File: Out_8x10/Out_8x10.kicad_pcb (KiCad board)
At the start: 2 copper layers, 100 x 100 mm, 162 parts, among them J1 Conn_01x06, J2 nmount SW Debug, J3 USB_C_Receptacle_USB2.0, J4 Conn_01x06, J5 Conn_01x09, J6 Conn_01x10, J7 Conn_01x09, J8 Conn_01x12, Q1 2N7002, Q10 AO3401A, Q11 AO3401A, Q12 AO3401A, Q13 2N7002, Q14 2N7002, Q15 AO3401A, Q16 AO3401A, Q17 AO3400A, Q18 AO3400A, Q19 AO3400A, Q2 2N7002, Q20 AO3400A, Q21 AO3400A, Q22 AO3400A, Q23 AO3400A, Q24 AO3400A, Q25 AO3400A, Q26 AO3400A, Q3 2N7002, Q4 AO3401A, Q5 AO3401A, Q6 AO3401A, Q7 2N7002, Q8 2N7002, Q9 2N7002, SW1 Reset, SW2 Boot, SW3 ADDRESS, U1 ADM3483, U10 L78L24_SOT89, U11 L78L24_SOT89, U12 L78L24_SOT89, U13 L78L24_SOT89, U2 W25Q128JVSIQ, U3 RP2040, U4 SN74AHCT1G125, U5 AP2112K-3.3, U6 L78L24_SOT89, U7 L78L24_SOT89, U8 L78L24_SOT89, U9 L78L24_SOT89, Y1 12MHz,18pF

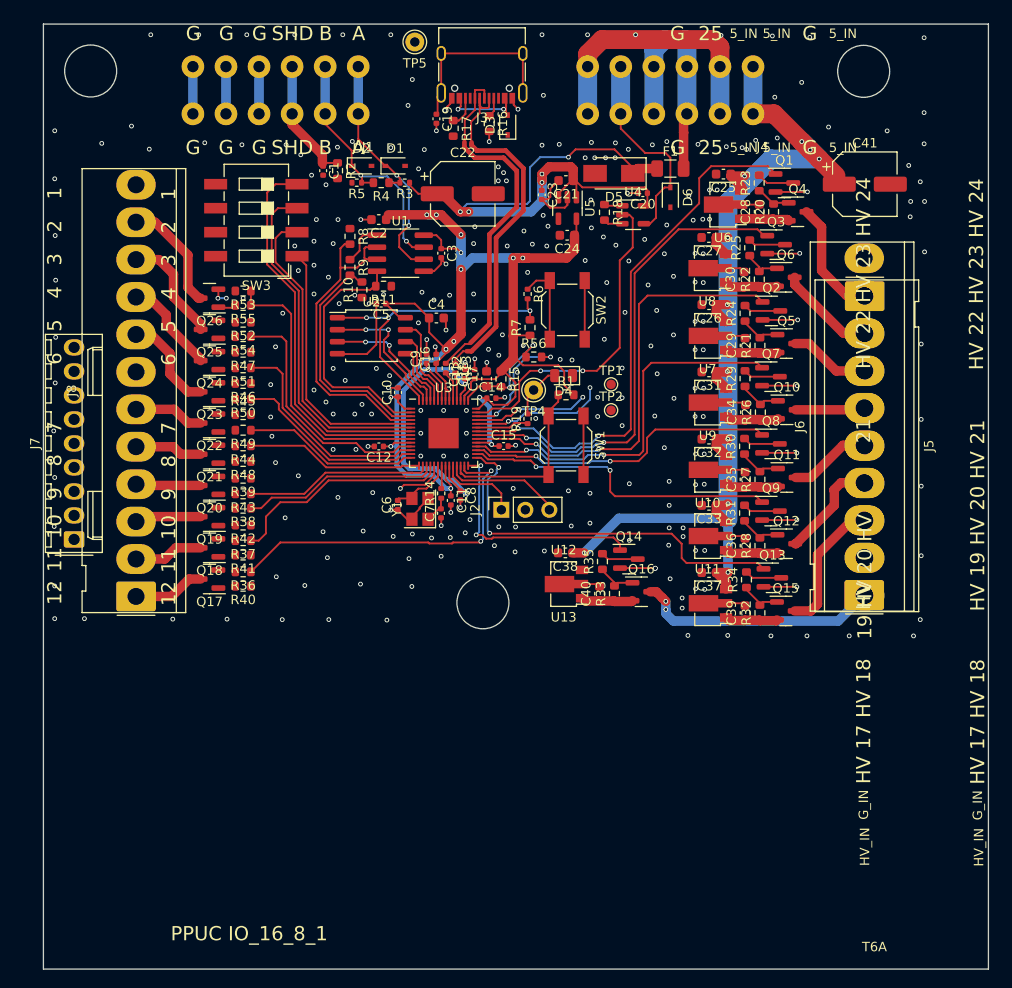
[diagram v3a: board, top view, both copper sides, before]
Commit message: updated layout
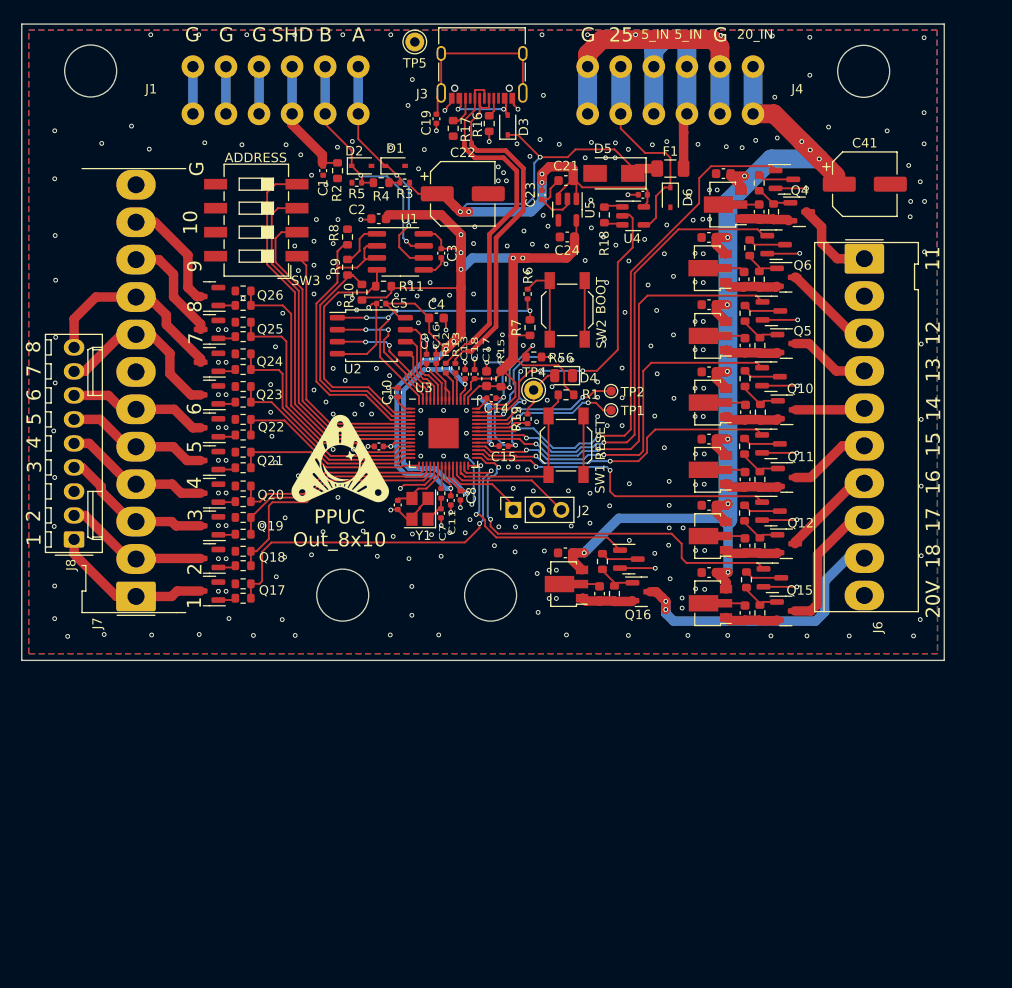
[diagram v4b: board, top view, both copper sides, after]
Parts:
- removed J5: Conn_01x09, Connector_Molex:Molex_KK-396_5273-09A_1x09_P3.96mm_Vertical
- added REF**: MountingHole_5.5mm_Pinball, IO_16_8_1:MountingHole_5.5mm_Pinball, F.Cu at (150.5, 105.2)
- moved J6 35.6 mm to (190.1, 69.6), turned to -90 degrees
- moved REF** 14.9 mm to (134.9, 105.2)
- moved TP1 2.74 mm to (163.3, 85.6)
- moved TP2 2.03 mm to (163.3, 83.6)
- moved Q17 1.27 mm to (120.8, 104.8)
- moved R36 1.27 mm to (124.3, 104.0)
- moved R40 1.27 mm to (124.3, 105.5)
- moved J2 1.26 mm to (152.9, 96.2)
- moved Q18 1.13 mm to (120.8, 101.3)
- moved R37 1.13 mm to (124.3, 100.6)
- moved R41 1.13 mm to (124.3, 102.1)
- moved Q19 0.98 mm to (120.8, 97.9)
- moved R38 0.98 mm to (124.3, 97.0)
- moved R42 0.98 mm to (124.3, 98.8)
- moved R43 0.82 mm to (124.3, 95.3)
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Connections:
- J6 pad 1: /Hi8/H8 -> /Hi8/H1
- J6 pad 10: /20V -> unconnected-(J6-Pad10)
- J6 pad 3: /Hi8/H7 -> /Hi8/H2
- J6 pad 4: /Hi8/H6 -> /Hi8/H3
- J6 pad 5: /Hi8/H5 -> /Hi8/H4
- J6 pad 6: /Hi8/H4 -> /Hi8/H5
- J6 pad 7: /Hi8/H3 -> /Hi8/H6
- J6 pad 8: /Hi8/H2 -> /Hi8/H7
- J6 pad 9: /Hi8/H1 -> /Hi8/H8
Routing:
- net GND: track 156.9 -> 181.9 mm, vias 276 -> 322
- net +3V3: track 146.0 -> 160.3 mm, vias 14 -> 12
- net /Lo10/L8: track 10.3 -> 21.0 mm
- net /Lo10/L1: track 7.60 -> 17.0 mm
- net /Lo10/L3: track 7.06 -> 16.3 mm
- net /Lo10/L7: track 10.6 -> 18.9 mm
- net /Lo10/L4: track 6.89 -> 14.9 mm
- net /Lo10/L5: track 7.17 -> 15.2 mm
- net /Lo10/L2: track 7.33 -> 15.3 mm
- net /Lo10/L6: track 7.44 -> 14.8 mm
- net +5V: track 66.9 -> 72.6 mm, vias 7 -> 5
- net /Hi8/H8: track 25.8 -> 30.6 mm
- net /Hi8/H1: track 12.5 -> 9.18 mm
- net Net-(TP2-Pad1): track 12.3 -> 15.6 mm
- net /Lo_2: track 23.8 -> 26.8 mm
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- added copper zone on B.Cu, net GND
- added copper zone on F.Cu, net GND
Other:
- board size 100 x 100 mm -> 97.6 x 67.3 mm
- board text added: "13"
- board text added: "14"
- board text added: "15"
- board text added: "16"
- board text added: "20V"
- board text added: "20_IN"
- board text added: "J5"
- board text added: "PPUC Out_8x10"
- board text added: "WPC connector"
- board text removed: "19"
- board text removed: "20"
- board text removed: "21"
- board text removed: "22"
- board text removed: "23"
- board text removed: "24"
- board text removed: "G_IN"
- board text removed: "HV"
- board text removed: "HV_IN"
- board text removed: "PPUC IO_16_8_1"
- board text removed: "T6A"

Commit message: Analog DIP
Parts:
- removed the REF** at (134.9, 105.2)
- added C42: 100n, Capacitor_SMD:C_0402_1005Metric, F.Cu at (142.4, 103.5)
- added R57: 2k, Resistor_SMD:R_0603_1608Metric, F.Cu at (140.3, 102.1)
- added R58: 1k, Resistor_SMD:R_0402_1005Metric, F.Cu at (138.0, 106.8)
- added R59: 5k, Resistor_SMD:R_0603_1608Metric, F.Cu at (134.5, 105.1)
- added R60: 2k, Resistor_SMD:R_0603_1608Metric, F.Cu at (134.5, 103.5)
- added R61: 2k, Resistor_SMD:R_0603_1608Metric, F.Cu at (134.5, 102.0)
- added R62: 1k, Resistor_SMD:R_0402_1005Metric, F.Cu at (134.4, 100.6)
- added R63: 3k, Resistor_SMD:R_0603_1608Metric, F.Cu at (137.5, 105.1)
- added R64: 2k, Resistor_SMD:R_0603_1608Metric, F.Cu at (137.5, 103.5)
- added TP3: TP_IO27, TestPoint:TestPoint_Pad_D1.0mm, F.Cu at (135.7, 98.0)
- added TP6: TP_IO27, TestPoint:TestPoint_Pad_D1.0mm, F.Cu at (136.8, 96.3)
- added TP7: TP_IO27, TestPoint:TestPoint_Pad_D1.0mm, F.Cu at (137.7, 98.1)
- added TP8: TP_IO27, TestPoint:TestPoint_Pad_D1.0mm, F.Cu at (150.7, 92.5)
- added U14: LMV321, Package_TO_SOT_SMD:SOT-23-5, F.Cu at (141.3, 105.8)
- R56: value 10k -> 33k
- Y1: value 12MHz,18pF -> 12MHz
- moved SW3 36.2 mm to (126.6, 101.8), turned to 90 degrees
- moved R56 25.2 mm to (142.8, 102.0), turned to 180 degrees
- moved Q17 12.2 mm to (121.1, 92.6)
- moved R36 12.2 mm to (124.6, 91.8)
- moved R40 12.2 mm to (124.6, 93.3)
- moved R43 12.2 mm to (124.6, 83.1)
- moved R46 12.2 mm to (124.6, 70.9)
- moved R53 12.2 mm to (124.6, 60.8)
- moved R55 12.2 mm to (124.6, 62.3)
- moved Q18 12.2 mm to (121.1, 89.1)
- moved Q19 12.2 mm to (121.1, 85.7)
- moved Q20 12.2 mm to (121.1, 82.2)
- moved Q21 12.2 mm to (121.1, 78.8)
- moved Q22 12.2 mm to (121.1, 75.3)
- moved Q23 12.2 mm to (121.1, 71.8)
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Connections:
- SW3 pad 1: /DIP_1 -> Net-(R58-Pad1)
- SW3 pad 2: /DIP_2 -> Net-(R60-Pad1)
- SW3 pad 3: /DIP_3 -> Net-(R60-Pad1)
- SW3 pad 4: /DIP_4 -> /V_addr
- SW3 pad 5: GND -> Net-(R63-Pad2)
- SW3 pad 6: GND -> Net-(R63-Pad2)
- SW3 pad 7: GND -> Net-(R61-Pad2)
- SW3 pad 8: GND -> Net-(R61-Pad2)
- U3 pad 11: /Lo_9 -> /Lo_5
- U3 pad 12: /Lo_8 -> /Lo_4
- U3 pad 13: /Lo_7 -> /Lo_3
- U3 pad 14: /Lo_6 -> /Lo_2
- U3 pad 15: /Lo_5 -> /Lo_1
- U3 pad 16: /Lo_4 -> Net-(U3-Pad16)
- U3 pad 17: /Lo_3 -> Net-(U3-Pad17)
- U3 pad 18: /Lo_2 -> Net-(U3-Pad18)
- U3 pad 27: /Lo_1 -> Net-(U3-Pad27)
- U3 pad 40: Net-(R56-Pad2) -> /V_addr
- U3 pad 5: /DIP_1 -> /Lo_10
- U3 pad 6: /DIP_2 -> /Lo_9
- U3 pad 7: /DIP_3 -> /Lo_8
- U3 pad 8: /DIP_4 -> /Lo_7
- U3 pad 9: /Lo_10 -> /Lo_6
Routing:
- net /V_addr: track 0.00 -> 43.0 mm, vias 0 -> 2
- net /DIP_4: track 40.8 -> 0.00 mm
- net /DIP_3: track 37.2 -> 0.00 mm
- net /DIP_2: track 33.6 -> 0.00 mm
- net Net-(R58-Pad1): track 0.00 -> 27.9 mm
- net /DIP_1: track 27.7 -> 0.00 mm
- net /Lo_1: track 40.1 -> 19.2 mm, vias 2 -> 0
- net /3V3A: track 12.3 -> 33.0 mm
- net Net-(R61-Pad2): track 0.00 -> 16.2 mm
- net Net-(R60-Pad1): track 0.00 -> 15.7 mm
- net Net-(R63-Pad2): track 0.00 -> 15.6 mm
- net Net-(U3-Pad16): track 0.00 -> 12.5 mm
- net Net-(U3-Pad18): track 0.00 -> 12.1 mm
- net /Lo_7: track 21.4 -> 32.5 mm
- net /Lo10/L1: track 17.0 -> 28.1 mm
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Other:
- board text added: "PPUC"

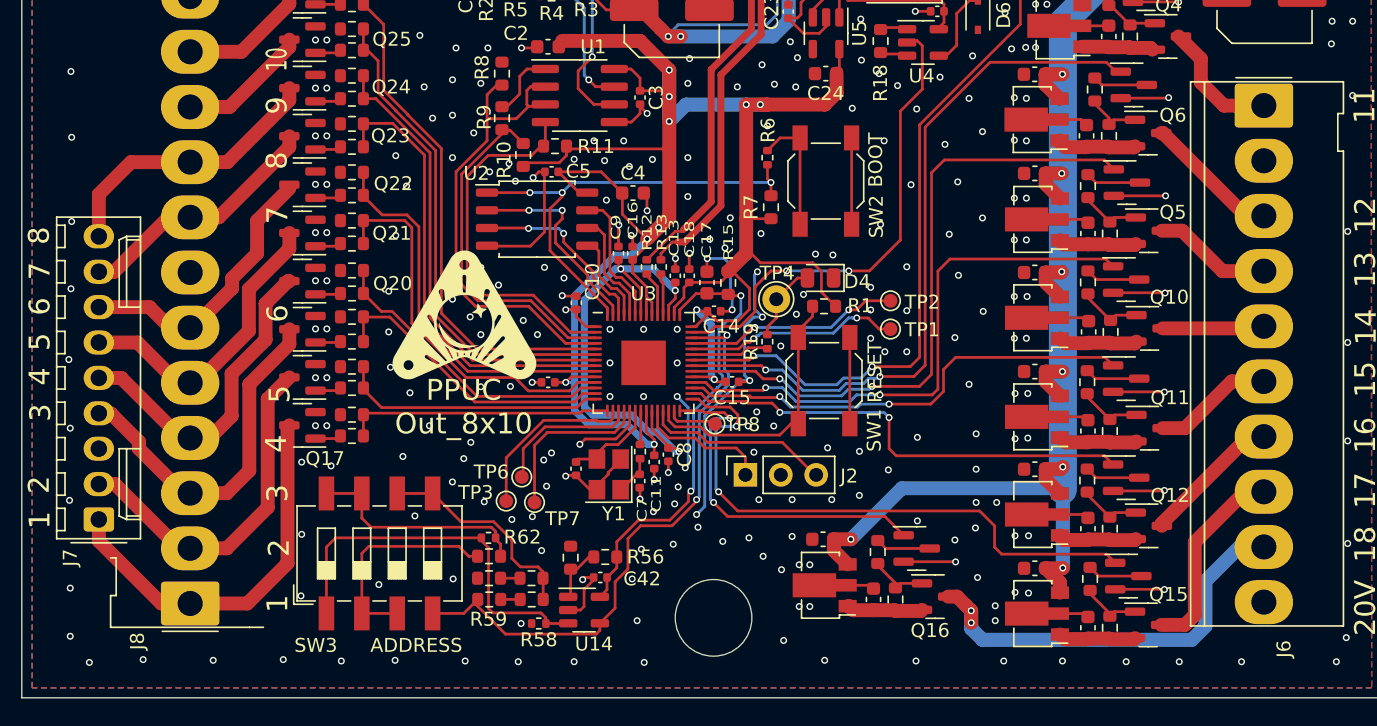
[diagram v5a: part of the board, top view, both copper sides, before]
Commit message: TPs to RM2.54
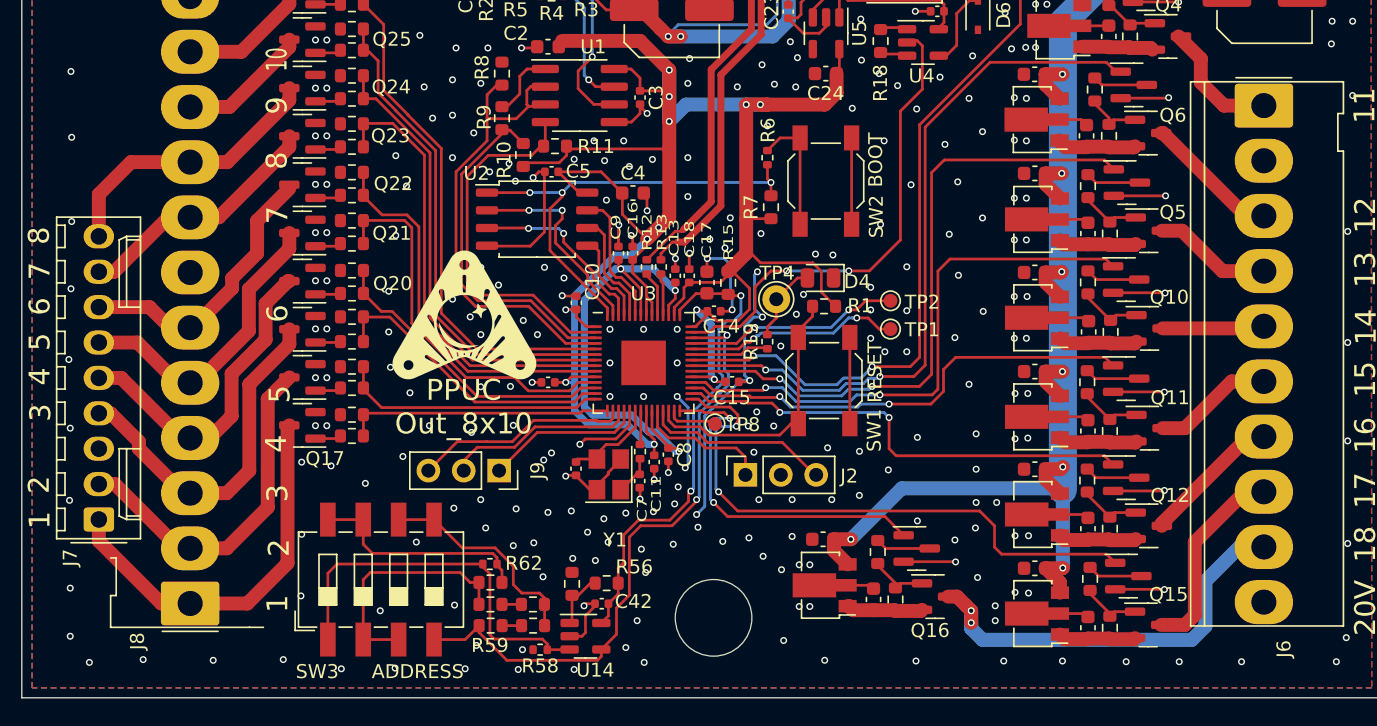
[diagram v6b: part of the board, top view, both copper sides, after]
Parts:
- removed TP3, TP6, TP7: TP_IO27, TestPoint:TestPoint_Pad_D1.0mm
- added J9: nmount TPs, Connector_PinSocket_2.54mm:PinSocket_1x03_P2.54mm_Vertical, F.Cu at (135.2, 95.8)
- Y1: value 12MHz -> 12MHz,18pF
- moved R57 1.88 mm to (140.4, 103.9)
- moved SW3 1.88 mm to (126.7, 103.6)
- moved C42 1.88 mm to (142.5, 105.4)
- moved R58 1.88 mm to (138.1, 108.7)
- moved R62 1.88 mm to (134.5, 102.5)
- moved R56 1.88 mm to (142.9, 103.9)
- moved R59 1.88 mm to (134.6, 106.9)
- moved R60 1.88 mm to (134.6, 105.4)
- moved R61 1.88 mm to (134.6, 103.8)
- moved R63 1.88 mm to (137.6, 106.9)
- moved R64 1.88 mm to (137.6, 105.4)
- moved U14 1.88 mm to (141.4, 107.7)
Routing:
- net Net-(J9-Pad2): track 10.5 -> 13.7 mm
- net Net-(J9-Pad3): track 12.5 -> 15.4 mm
- net /3V3A: track 33.0 -> 34.8 mm
- net /V_addr: track 43.0 -> 44.8 mm
- net Net-(R60-Pad1): track 15.7 -> 17.2 mm
- net Net-(J9-Pad1): track 12.1 -> 11.3 mm
- net GND: track 190.9 -> 190.8 mm, vias 337 -> 349

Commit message: V1.0.0
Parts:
- removed F1: T500mA,<0.3Ω, Fuse:Fuse_1206_3216Metric
- removed R3, R5: 1k, Resistor_SMD:R_0402_1005Metric
- added D7: 1A, Diode_SMD:D_SOD-323, F.Cu at (169.5, 60.1)
- added JP1: Jumper_2_Open, Connector_PinHeader_2.54mm:PinHeader_1x02_P2.54mm_Vertical, F.Cu at (141.6, 55.5)
- moved D1 0.17 mm to (140.6, 59.8)
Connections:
- J1 pad 4: GND -> /A
- J1 pad 5: GND -> /B
- R4 pad 1: /A -> Net-(JP1-Pad1)
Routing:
- net /A: track 27.0 -> 49.3 mm
- net /B: track 27.8 -> 45.1 mm
- net GND: track 190.8 -> 180.8 mm
- net Net-(JP1-Pad1): track 0.00 -> 6.83 mm
- net +5V: track 72.6 -> 69.3 mm
- net /5V_IN: track 23.8 -> 24.6 mm
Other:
- rule pad_to_mask_clearance: 0 -> 0.05
